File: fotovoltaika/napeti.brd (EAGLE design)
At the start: 25.1 x 39.4 mm, 6 parts

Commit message: upravy desek
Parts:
- removed JP1: (no value), jumper:JP2
- removed SL2: (no value), con-amp-quick:04P
- removed SL3, SL4, SL5: (no value), con-amp-quick:03P
- added ADC11150X48, ADC11150X49: (no value), con-amp-quick:10P
- added R1, R3, R5: 10k, rcl:0204/7
- added R2: 2k7, rcl:0204/7
- added R4, R6: 4k7, rcl:0204/7
- added R7, R8: (no value), rcl:0204/7
- added X1, X2, X3, X4: (no value), con-wago-500:W237-102
- SL1: device con-amp-quick:10P -> con-amp-quick:04P
- moved SL1 37.5 mm to (40.6, 39.4), turned to 270 degrees
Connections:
- removed net +5V: JP1.1, SL1.10, SL2.1, SL3.2, SL4.2, SL5.2
- removed net N$11: SL1.7, SL2.4
- new net 5V: ADC11150X48.10, ADC11150X49.10, ADC11150X49.6, SL1.1
- new net N$1: ADC11150X48.1, R5.2, R6.2
- new net N$10: ADC11150X49.2, R2.1, X1.2
- new net N$13: ADC11150X49.3, R3.2, R4.2
- new net N$3: ADC11150X48.2, R6.1, X3.2
- new net N$4: ADC11150X48.3, R7.2, R8.2
- new net N$8: R7.1, X4.1
- new net N$9: ADC11150X49.1, R1.2, R2.2
- new net SCL: ADC11150X48.5, ADC11150X48.7, ADC11150X49.7, SL1.4
- new net SDA: ADC11150X48.8, ADC11150X49.5, ADC11150X49.8, SL1.3
- net GND: now also ADC11150X48.6, ADC11150X48.9, ADC11150X49.9, SL1.2; no longer JP1.3, SL1.9, SL2.2, SL3.1, SL4.1, SL5.1
- net N$14: now also ADC11150X49.4, R4.1, X2.2; no longer JP1.2, SL1.6
- net N$2: now also R1.1, X1.1; no longer SL1.8, SL2.3
- net N$5: now also R3.1, X2.1; no longer SL1.2, SL3.3
- net N$6: now also ADC11150X48.4, R8.1, X4.2; no longer SL1.3, SL4.3
- net N$7: now also R5.1, X3.1; no longer SL1.4, SL5.3
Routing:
- net 5V: track 0.00 -> 129.3 mm
- net +5V: track 42.7 -> 0.00 mm
- net SDA: track 0.00 -> 39.2 mm
- net SCL: track 0.00 -> 34.3 mm
- net N$6: track 7.93 -> 32.6 mm
- net N$4: track 0.00 -> 23.9 mm
- net N$13: track 0.00 -> 23.9 mm
- net N$14: track 8.89 -> 32.6 mm
- net N$3: track 0.00 -> 23.2 mm
- net N$10: track 0.00 -> 23.2 mm
- net N$9: track 0.00 -> 11.2 mm
- net N$1: track 0.00 -> 11.2 mm
- net GND: track 32.8 -> 43.2 mm
- net N$8: track 0.00 -> 5.10 mm
- net N$11: track 5.08 -> 0.00 mm
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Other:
- board size 25.1 x 39.4 mm -> 46.7 x 49.5 mm

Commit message: + displej
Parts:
- renumbered ADC11150X48 to ADC11150X4A, ADC11150X49 to ADC11150X4B
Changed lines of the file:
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@@
 <?xml version="1.0" encoding="utf-8"?>
 <!DOCTYPE eagle SYSTEM "eagle.dtd">
-<eagle version="9.3.0">
+<eagle version="9.4.1">
 <drawing>
 <settings>
@@
 </autorouter>
 <elements>
-<element name="ADC11150X48" library="con-amp-quick" library_urn="urn:adsk.eagle:library:125" package="10P" package3d_urn="urn:adsk.eagle:package:5963/1" value="" x="35.56" y="31.75" smashed="yes" rot="R90">
+<element name="ADC11150X4A" library="con-amp-quick" library_urn="urn:adsk.eagle:library:125" package="10P" package3d_urn="urn:adsk.eagle:package:5963/1" value="" x="35.56" y="31.75" smashed="yes" rot="R90">
 <attribute name="MF" value="" x="48.26" y="57.15" size="1.778" layer="27" rot="R90" display="off"/>
 <attribute name="MPN" value="" x="48.26" y="57.15" size="1.778" layer="27" rot="R90" display="off"/>
@@
 <attribute name="VALUE" x="39.3954" y="19.304" size="1.27" layer="27" ratio="10" rot="R90"/>
 </element>
-<element name="ADC11150X49" library="con-amp-quick" library_urn="urn:adsk.eagle:library:125" package="10P" package3d_urn="urn:adsk.eagle:package:5963/1" value="" x="15.24" y="31.75" smashed="yes" rot="R90">
+<element name="ADC11150X4B" library="con-amp-quick" library_urn="urn:adsk.eagle:library:125" package="10P" package3d_urn="urn:adsk.eagle:package:5963/1" value="" x="15.24" y="31.75" smashed="yes" rot="R90">
 <attribute name="MF" value="" x="35.56" y="57.15" size="1.778" layer="27" rot="R90" display="off"/>
 <attribute name="MPN" value="" x="35.56" y="57.15" size="1.778" layer="27" rot="R90" display="off"/>
@@
 <signals>
 <signal name="5V">
-<contactref element="ADC11150X49" pad="10"/>
+<contactref element="ADC11150X4B" pad="10"/>
 <contactref element="SL1" pad="1"/>
-<contactref element="ADC11150X48" pad="10"/>
-<contactref element="ADC11150X49" pad="6"/>
+<contactref element="ADC11150X4A" pad="10"/>
+<contactref element="ADC11150X4B" pad="6"/>
 <wire x1="35.56" y1="43.18" x2="15.24" y2="43.18" width="0.8128" layer="16"/>
 <wire x1="40.64" y1="43.18" x2="35.56" y2="43.18" width="0.8128" layer="16"/>
@@
 </signal>
 <signal name="GND">
-<contactref element="ADC11150X49" pad="9"/>
+<contactref element="ADC11150X4B" pad="9"/>
 <contactref element="SL1" pad="2"/>
-<contactref element="ADC11150X48" pad="9"/>
-<contactref element="ADC11150X48" pad="6"/>
+<contactref element="ADC11150X4A" pad="9"/>
+<contactref element="ADC11150X4A" pad="6"/>
 <wire x1="40.64" y1="40.64" x2="43.18" y2="40.64" width="0.8128" layer="16"/>
 <wire x1="43.18" y1="40.64" x2="43.18" y2="33.02" width="0.8128" layer="16"/>
@@
 </signal>
 <signal name="SDA">
-<contactref element="ADC11150X49" pad="8"/>
+<contactref element="ADC11150X4B" pad="8"/>
 <contactref element="SL1" pad="3"/>
-<contactref element="ADC11150X48" pad="8"/>
+<contactref element="ADC11150X4A" pad="8"/>
 <wire x1="35.56" y1="38.1" x2="15.24" y2="38.1" width="0.8128" layer="16"/>
 <wire x1="40.64" y1="38.1" x2="35.56" y2="38.1" width="0.8128" layer="16"/>
-<contactref element="ADC11150X49" pad="5"/>
+<contactref element="ADC11150X4B" pad="5"/>
 <wire x1="15.24" y1="30.48" x2="12.7" y2="30.48" width="0.8128" layer="16"/>
 <wire x1="12.7" y1="30.48" x2="11.43" y2="31.75" width="0.8128" layer="16"/>
@@
 </signal>
 <signal name="SCL">
-<contactref element="ADC11150X49" pad="7"/>
+<contactref element="ADC11150X4B" pad="7"/>
 <contactref element="SL1" pad="4"/>
-<contactref element="ADC11150X48" pad="7"/>
+<contactref element="ADC11150X4A" pad="7"/>
 <wire x1="35.56" y1="35.56" x2="31.75" y2="35.56" width="0.8128" layer="16"/>
 <wire x1="31.75" y1="35.56" x2="15.24" y2="35.56" width="0.8128" layer="16"/>
 <wire x1="40.64" y1="35.56" x2="35.56" y2="35.56" width="0.8128" layer="16"/>
-<contactref element="ADC11150X48" pad="5"/>
+<contactref element="ADC11150X4A" pad="5"/>
 <wire x1="35.56" y1="30.48" x2="31.75" y2="30.48" width="0.8128" layer="16"/>
 <wire x1="31.75" y1="30.48" x2="31.75" y2="35.56" width="0.8128" layer="16"/>
 </signal>
 <signal name="N$9">
-<contactref element="ADC11150X49" pad="1"/>
+<contactref element="ADC11150X4B" pad="1"/>
 <contactref element="R1" pad="2"/>
 <contactref element="R2" pad="2"/>
@@
 </signal>
 <signal name="N$10">
-<contactref element="ADC11150X49" pad="2"/>
+<contactref element="ADC11150X4B" pad="2"/>
 <contactref element="R2" pad="1"/>
 <wire x1="12.7" y1="17.78" x2="12.7" y2="22.86" width="0.8128" layer="16"/>
@@
 </signal>
 <signal name="N$13">
-<contactref element="ADC11150X49" pad="3"/>
+<contactref element="ADC11150X4B" pad="3"/>
 <contactref element="R3" pad="2"/>
 <contactref element="R4" pad="2"/>
@@
 </signal>
 <signal name="N$14">
-<contactref element="ADC11150X49" pad="4"/>
+<contactref element="ADC11150X4B" pad="4"/>
 <contactref element="R4" pad="1"/>
 <wire x1="5.08" y1="17.78" x2="5.08" y2="25.4" width="0.8128" layer="16"/>
@@
 <contactref element="R5" pad="2"/>
 <contactref element="R6" pad="2"/>
-<contactref element="ADC11150X48" pad="1"/>
+<contactref element="ADC11150X4A" pad="1"/>
 <wire x1="35.56" y1="17.78" x2="35.56" y2="12.7" width="0.8128" layer="16"/>
 <wire x1="33.02" y1="10.16" x2="35.56" y2="12.7" width="0.8128" layer="16"/>
@@
 <signal name="N$3">
 <contactref element="R6" pad="1"/>
-<contactref element="ADC11150X48" pad="2"/>
+<contactref element="ADC11150X4A" pad="2"/>
 <wire x1="33.02" y1="17.78" x2="33.02" y2="22.86" width="0.8128" layer="16"/>
 <wire x1="33.02" y1="22.86" x2="35.56" y2="22.86" width="0.8128" layer="16"/>
@@
 <contactref element="R7" pad="2"/>
 <contactref element="R8" pad="2"/>
-<contactref element="ADC11150X48" pad="3"/>
+<contactref element="ADC11150X4A" pad="3"/>
 <wire x1="27.94" y1="17.78" x2="27.94" y2="12.7" width="0.8128" layer="16"/>
 <wire x1="25.4" y1="10.16" x2="27.94" y2="12.7" width="0.8128" layer="16"/>
@@
 <signal name="N$6">
 <contactref element="R8" pad="1"/>
-<contactref element="ADC11150X48" pad="4"/>
+<contactref element="ADC11150X4A" pad="4"/>
 <wire x1="25.4" y1="17.78" x2="25.4" y2="25.4" width="0.8128" layer="16"/>
 <wire x1="25.4" y1="25.4" x2="27.94" y2="27.94" width="0.8128" layer="16"/>

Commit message: prodloužení intervalu sepnutí relé na 1 hodinu dělení proudu 2, nevím proč vychází proud 2x více než ve skutečnosti je, zjistit
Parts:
- R1: value 10k -> 15k
- R2: value 2k7 -> 4k7
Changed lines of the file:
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@@
 <?xml version="1.0" encoding="utf-8"?>
 <!DOCTYPE eagle SYSTEM "eagle.dtd">
-<eagle version="9.4.1">
+<eagle version="9.4.2">
 <drawing>
 <settings>
@@
 <attribute name="VALUE" x="19.0754" y="19.304" size="1.27" layer="27" ratio="10" rot="R90"/>
 </element>
-<element name="R1" library="rcl" library_urn="urn:adsk.eagle:library:334" package="0204/7" package3d_urn="urn:adsk.eagle:package:23498/1" value="10k" x="15.24" y="13.97" smashed="yes" rot="R90">
+<element name="R1" library="rcl" library_urn="urn:adsk.eagle:library:334" package="0204/7" package3d_urn="urn:adsk.eagle:package:23498/1" value="15k" x="15.24" y="13.97" smashed="yes" rot="R90">
 <attribute name="NAME" x="13.9446" y="11.43" size="0.9906" layer="25" ratio="10" rot="R90"/>
 <attribute name="SPICEPREFIX" value="R" x="41.91" y="48.26" size="1.778" layer="27" rot="R90" display="off"/>
 <attribute name="VALUE" x="15.7226" y="12.3444" size="0.9906" layer="27" ratio="10" rot="R90"/>
 </element>
-<element name="R2" library="rcl" library_urn="urn:adsk.eagle:library:334" package="0204/7" package3d_urn="urn:adsk.eagle:package:23498/1" value="2k7" x="12.7" y="13.97" smashed="yes" rot="R270">
+<element name="R2" library="rcl" library_urn="urn:adsk.eagle:library:334" package="0204/7" package3d_urn="urn:adsk.eagle:package:23498/1" value="4k7" x="12.7" y="13.97" smashed="yes" rot="R270">
 <attribute name="NAME" x="13.9954" y="16.51" size="0.9906" layer="25" ratio="10" rot="R270"/>
 <attribute name="SPICEPREFIX" value="R" x="-21.59" y="-3.81" size="1.778" layer="27" rot="R270" display="off"/>

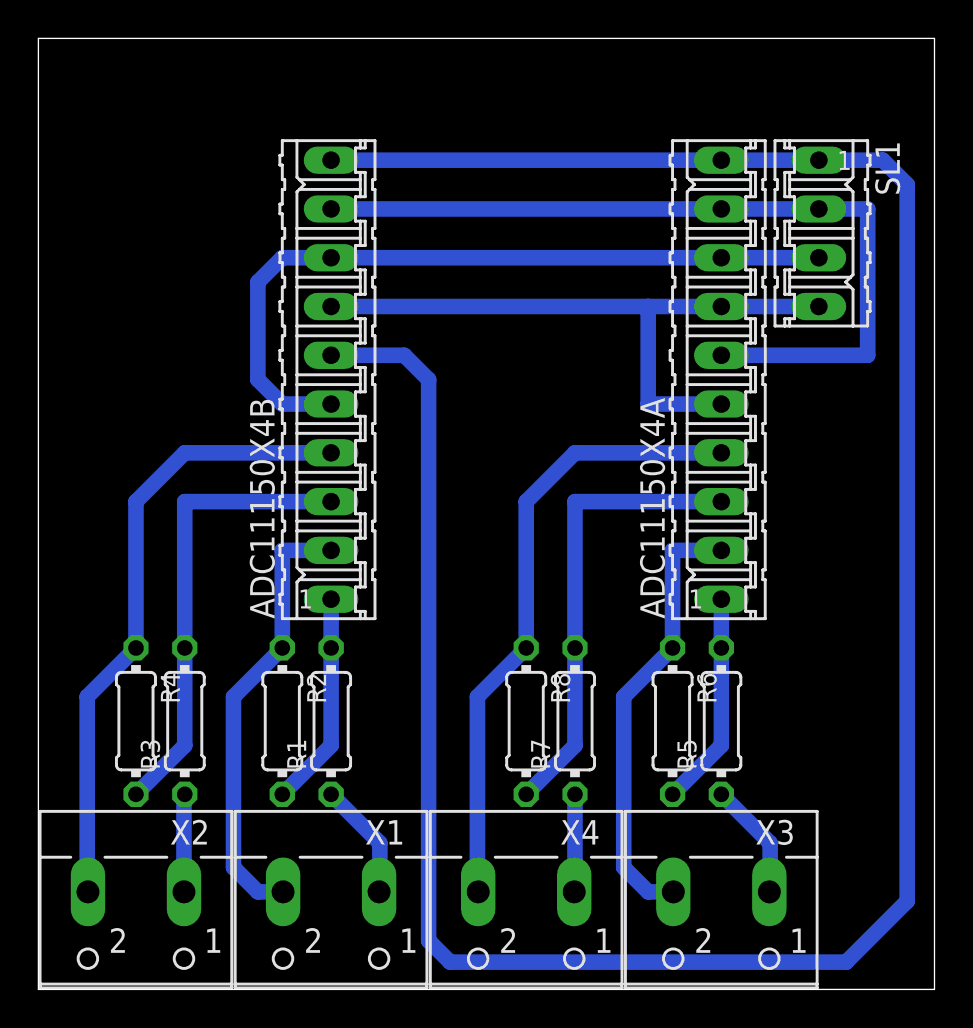
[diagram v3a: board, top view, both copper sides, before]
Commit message: uprava desky pro mereni napeti pro JST-XH konektor
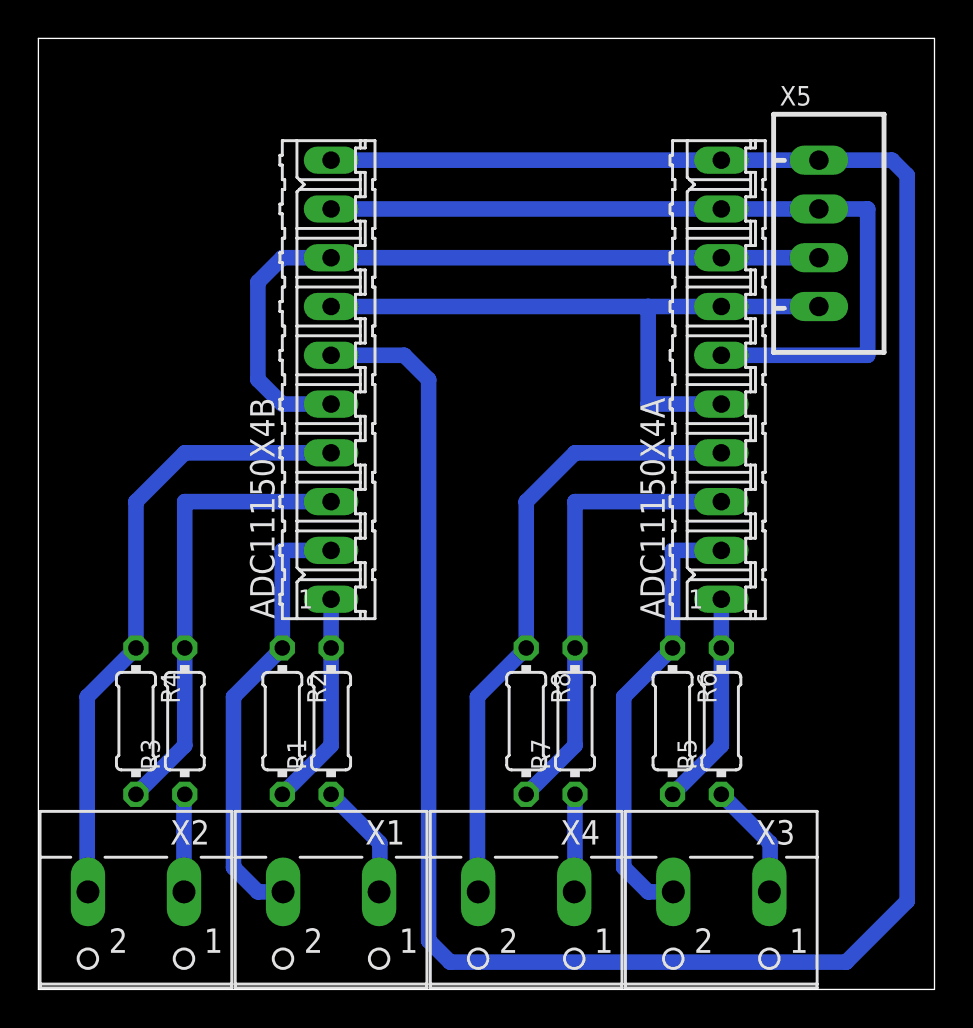
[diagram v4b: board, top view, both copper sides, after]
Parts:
- removed SL1: (no value), con-amp-quick:04P
- added X5: JST-XH-04-PIN-LONG-PAD, Rembrandt:JST-XH-04-PACKAGE-LONG-PAD
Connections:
- net 5V: now also X5.1; no longer SL1.1
- net GND: now also X5.2; no longer SL1.2
- net SCL: now also X5.4; no longer SL1.4
- net SDA: now also X5.3; no longer SL1.3
